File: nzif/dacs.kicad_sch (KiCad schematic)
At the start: 1 part, among them U5 ADAU1966AWBSTZ

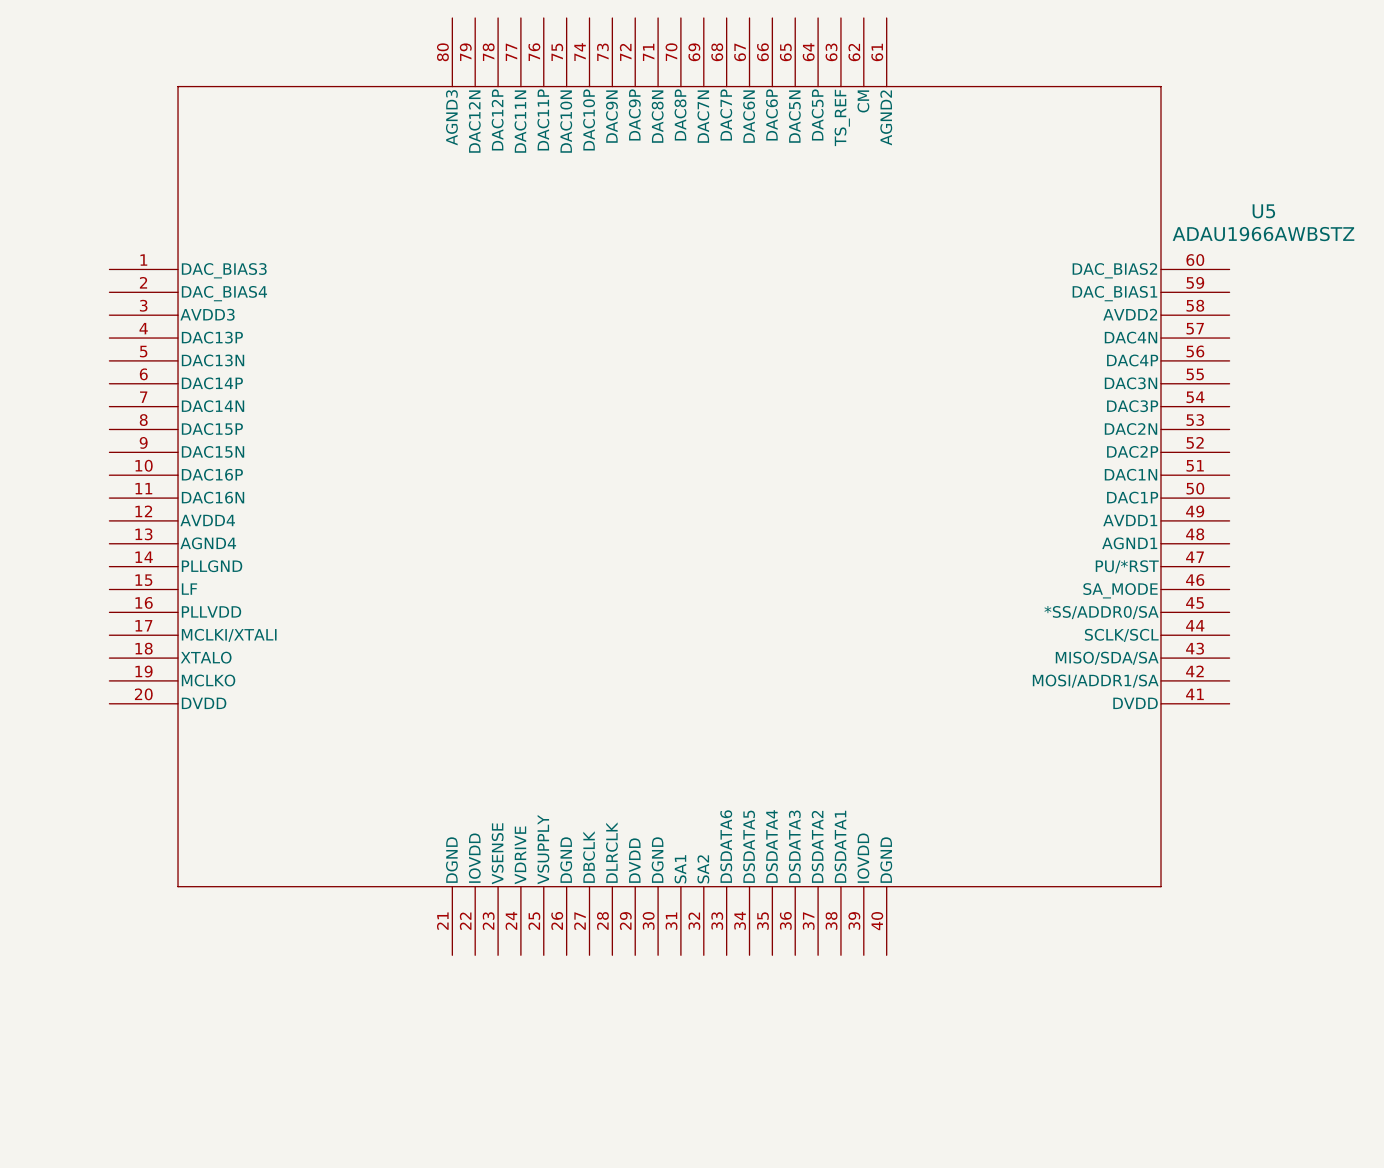
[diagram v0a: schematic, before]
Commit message: Add KLC Compliant DAC (ref #2) - update ADC readme
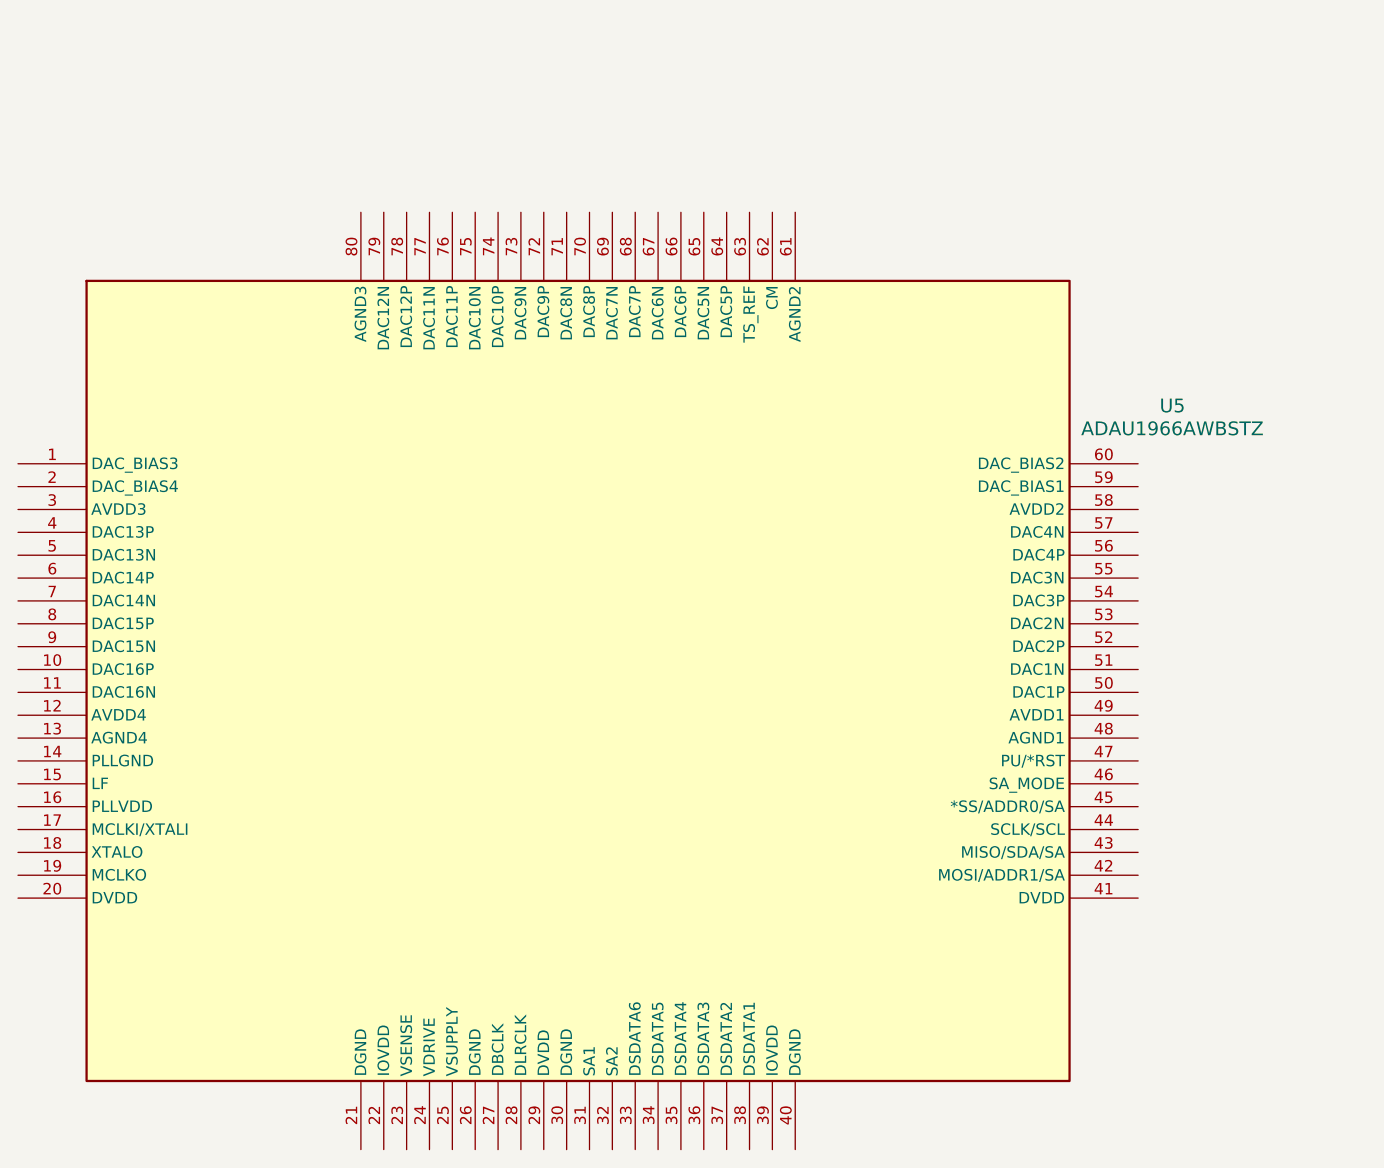
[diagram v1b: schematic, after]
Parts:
- U5: footprint ST_80_2_ADI -> nzif_footprints:ST_80_2_ADI; symbol ADAU1966:ADAU1966AWBSTZ -> nzif_radio_symbol_library:ADAU1966AWBSTZ
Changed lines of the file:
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@@
 	)
 	(symbol
-		(lib_id "ADAU1966:ADAU1966AWBSTZ")
-		(at 143.51 92.71 0)
+		(lib_id "nzif_radio_symbol_library:ADAU1966AWBSTZ")
+		(at 195.58 138.43 0)
 		(unit 1)
 		(exclude_from_sim no)
@@
 		(fields_autoplaced yes)
 		(property "Reference" "U5"
-			(at 271.78 86.2898 0)
+			(at 261.62 107.8798 0)
 			(effects
 				(font
@@
 		)
 		(property "Value" "ADAU1966AWBSTZ"
-			(at 271.78 88.8298 0)
+			(at 261.62 110.4198 0)
 			(effects
 				(font
@@
 			)
 		)
-		(property "Footprint" "ST_80_2_ADI"
-			(at 143.51 92.71 0)
+		(property "Footprint" "nzif_footprints:ST_80_2_ADI"
+			(at 195.58 138.43 0)
 			(effects
 				(font
@@
 		)
 		(property "Datasheet" "https://www.analog.com/media/en/technical-documentation/data-sheets/ADAU1966A.pdf"
-			(at 143.51 92.71 0)
+			(at 195.58 138.43 0)
 			(effects
 				(font
@@
 			)
 		)
-		(property "Description" ""
-			(at 143.51 92.71 0)
+		(property "Description" "16-Channel High Performance Audio DAC, 112dB SNR, I2C/SPI Control, ST-80-2"
+			(at 195.58 138.43 0)
 			(effects
 				(font

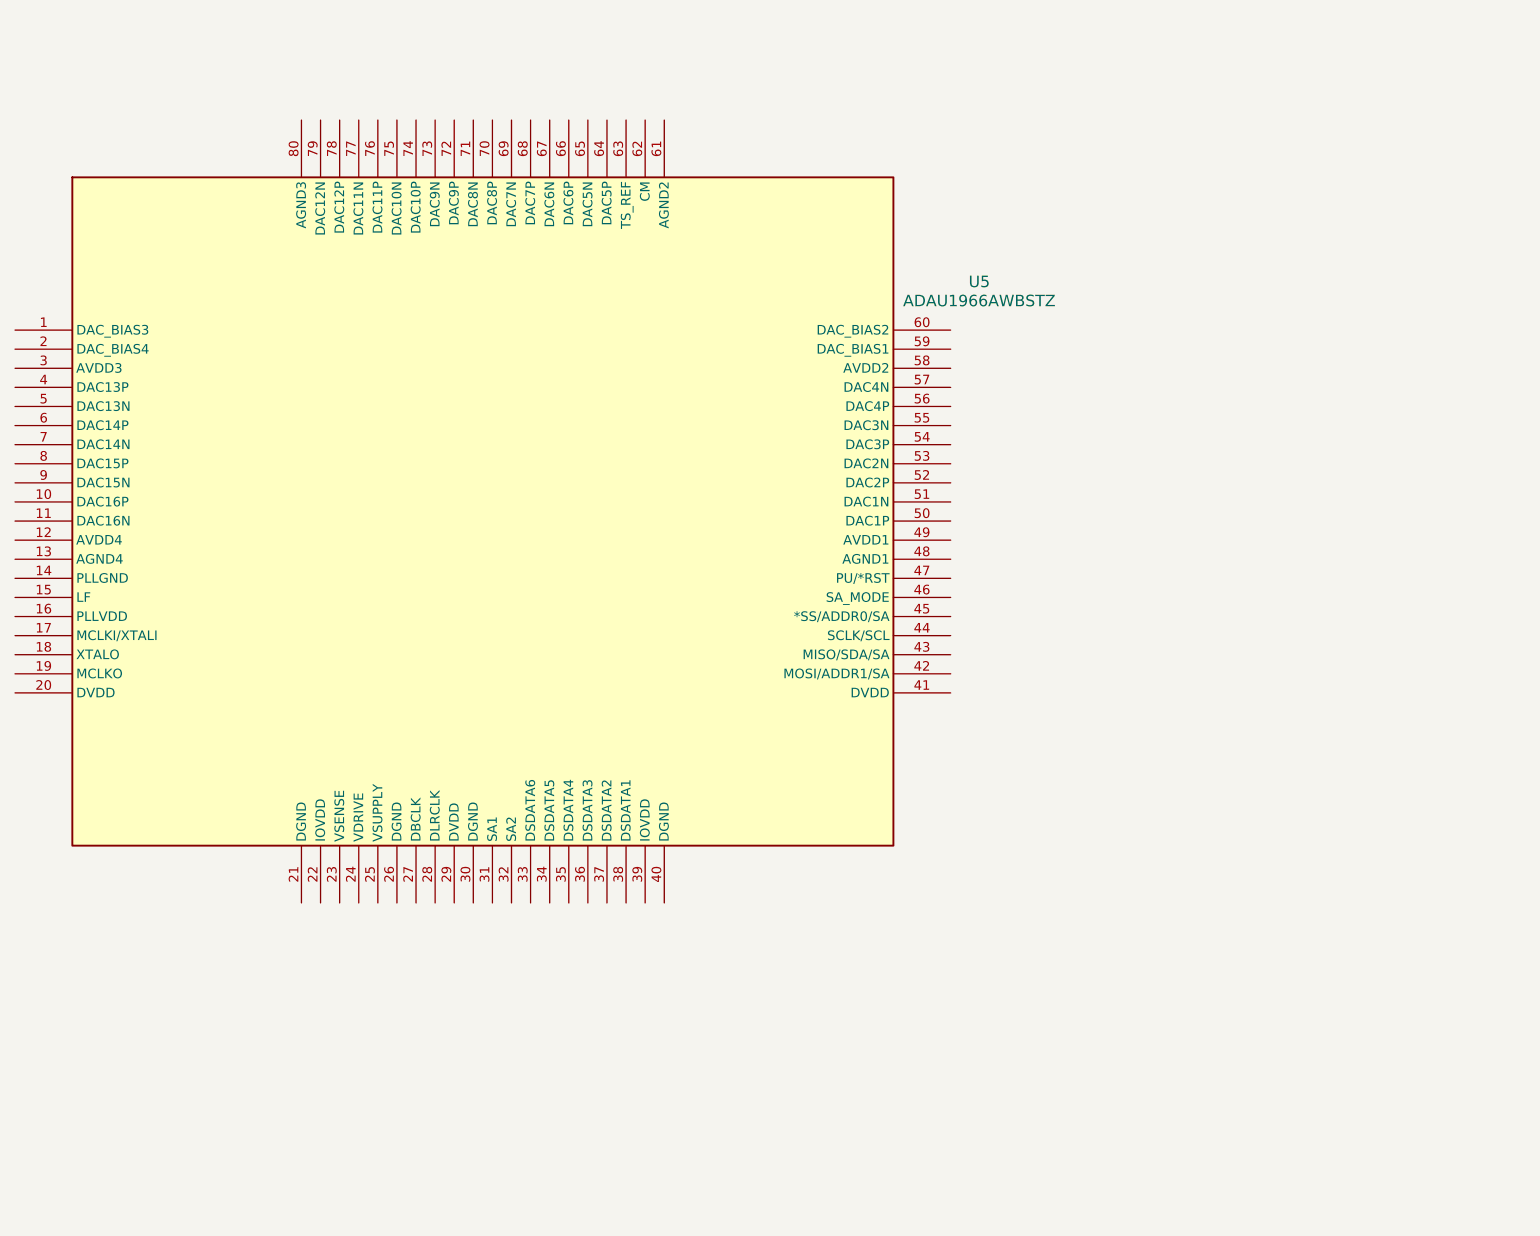
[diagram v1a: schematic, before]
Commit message: updates to DAC and DSP symbols (#2 and #3)
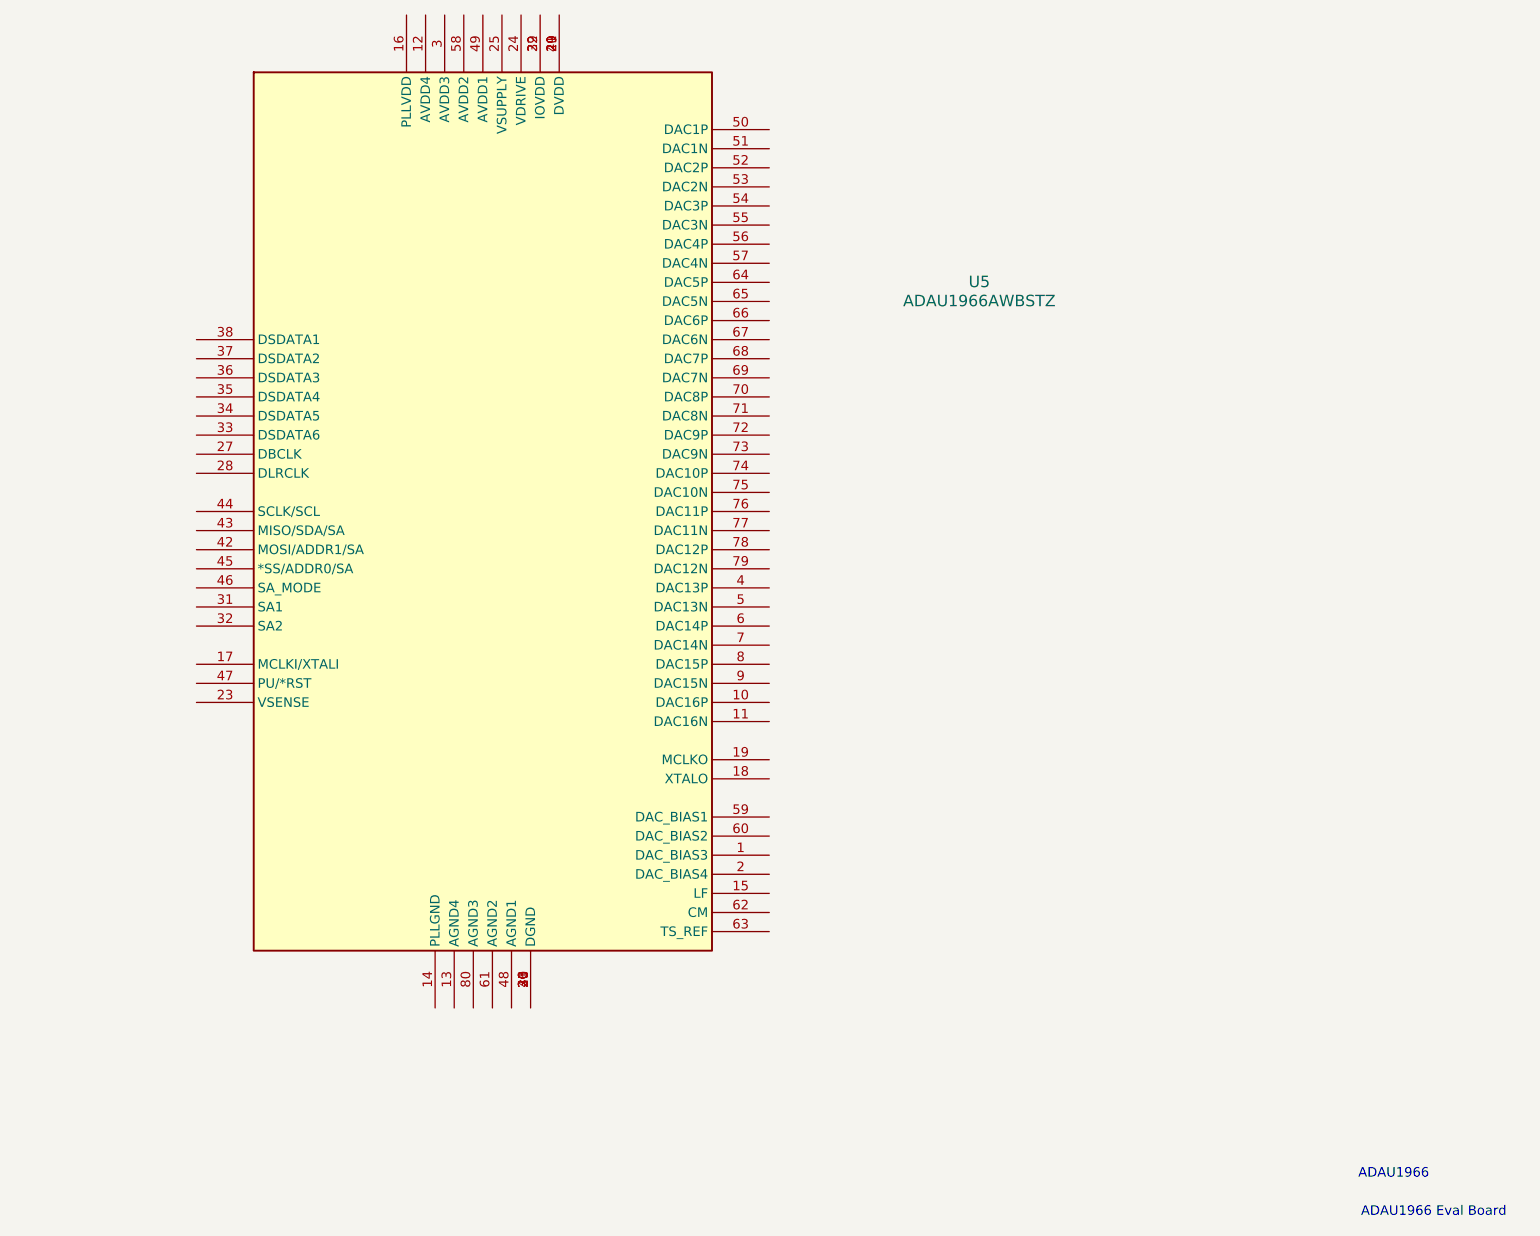
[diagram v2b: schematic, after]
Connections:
- net at U5.20 (DVDD): now also U5.29 (DVDD), U5.41 (DVDD)
- net at U5.21 (DGND): now also U5.26 (DGND), U5.30 (DGND), U5.40 (DGND)
- net at U5.22 (IOVDD): now also U5.39 (IOVDD)
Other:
- note added: "ADAU1966"
- note added: "ADAU1966 Eval Board"
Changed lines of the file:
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@@
 		(company "Andy McCann KA3KAF and Doug McCann KA3KAG")
+	)
+	(text "ADAU1966"
+		(exclude_from_sim no)
+		(at 316.738 226.568 0)
+		(effects
+			(font
+				(size 1.27 1.27)
+			)
+			(href "https://www.analog.com/en/products/adau1966a.html?doc=ADAU1966A.pdf")
+		)
+	)
+	(text "ADAU1966 Eval Board"
+		(exclude_from_sim no)
+		(at 322.072 231.648 0)
+		(effects
+			(font
+				(size 1.27 1.27)
+			)
+			(href "https://www.analog.com/media/en/technical-documentation/user-guides/UG-564.pdf")
+		)
 	)
 	(symbol
@@
 		)
 		(instances
+			(project "dacs"
+				(path "/2de56439-3342-4514-bfd7-22b434f17500"
+					(reference "U?")
+					(unit 1)
+				)
+			)
 			(project ""
 				(path "/fe42ca2f-2bb8-4d5a-9e84-807788ed632f/1097e363-2947-4914-97f0-a09e0bb38c3a"
@@
 		)
 	)
+	(sheet_instances
+		(path "/"
+			(page "1")
+		)
+	)
+	(embedded_fonts no)
 )
